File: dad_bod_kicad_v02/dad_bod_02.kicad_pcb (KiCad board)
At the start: 2 copper layers, 79.8 x 79.5 mm, 87 parts, among them J1 Conn_01x01, J10 Conn_01x03_Male, J11 BNC5-J-P-GN-RA-BH2D, J2 Conn_01x01, J3 Conn_01x01, J4 Conn_01x01, J5 BNC5-J-P-GN-RA-BH2D, J6 Conn_02x15_Odd_Even, J7 Conn_01x03_Male, J8 Conn_01x03_Male, K1 EC2-5NU, K2 EC2-5NU, Q1 2N3904, Q2 2N3904, T1 GT07-110-013, U1 SL1002A600SP

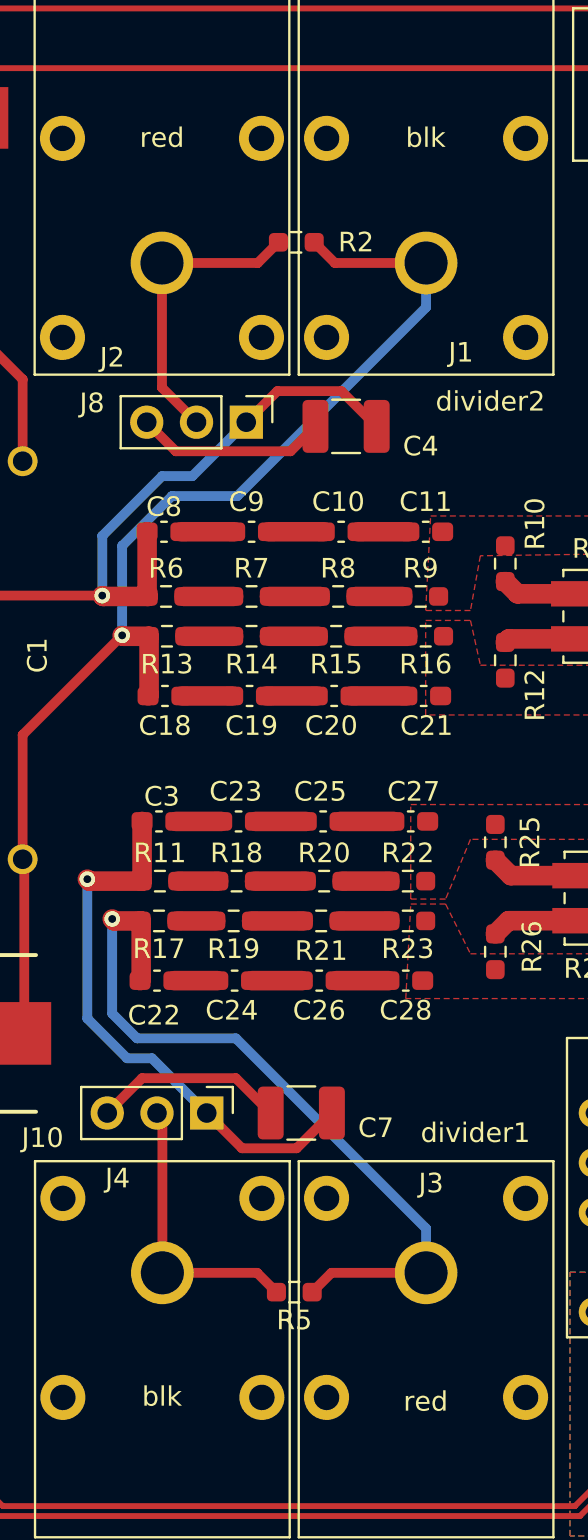
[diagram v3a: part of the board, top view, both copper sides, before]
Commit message: added notes to v02 after build
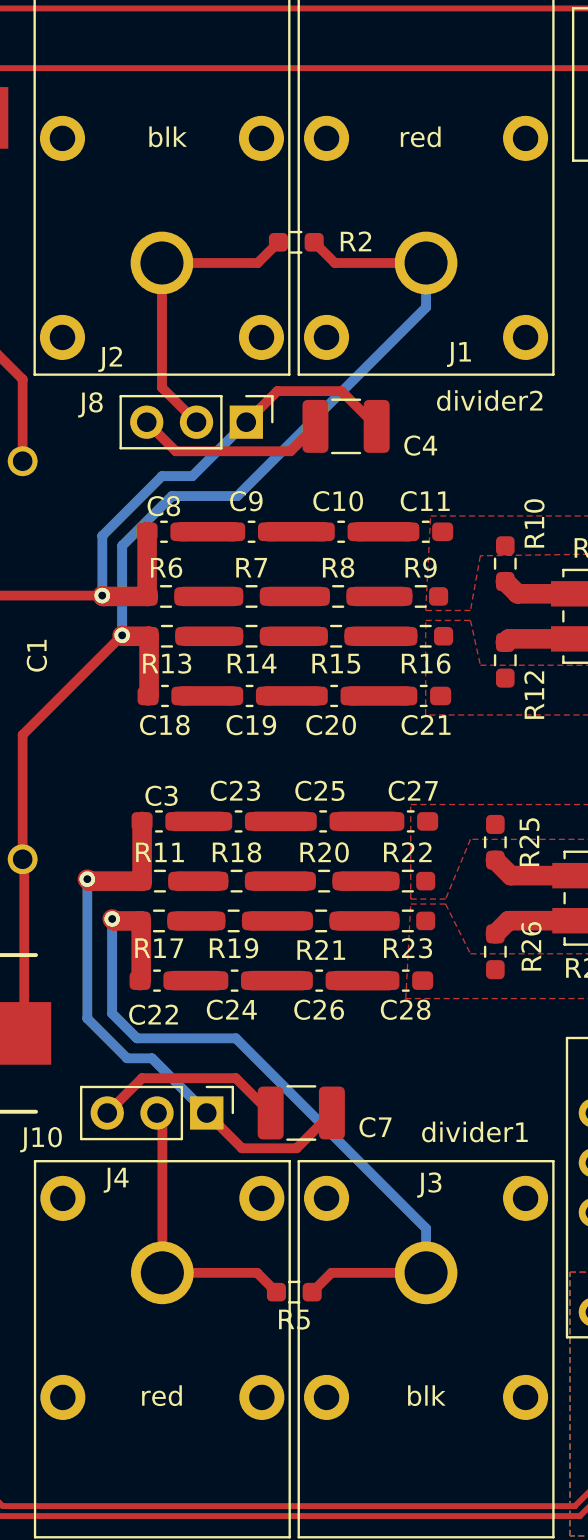
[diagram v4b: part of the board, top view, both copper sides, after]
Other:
- board text added: "corners might need chamfered, 8.5mm"
- board text added: "drill holes for standoffs to attach to case, standoffs need to be at least 13.5mm to clear C1"
- board text added: "increase clearance on dividers"
- board text added: "push header back to match dad"
- board text added: "r2 r5 r27 need 0803"
- board text added: "red/blk have been reversed because this board is flipped upside down when installed"
- board text added: "rotate d1"
- board text added: "translate dad mounting holes to this board, so they can be connected with stand-offs"
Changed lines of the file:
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@@
     (effects (font (size 1 1) (thickness 0.15)) (justify left))
   )
-  (gr_text "blk" (at 134.112 70.866) (layer "F.SilkS")
+  (gr_text "blk" (at 120.904 70.866) (layer "F.SilkS")
     (effects (font (size 1 1) (thickness 0.15)))
   )
@@
     (effects (font (size 1 1) (thickness 0.15)))
   )
-  (gr_text "blk" (at 120.65 135.128) (layer "F.SilkS")
+  (gr_text "blk" (at 134.112 135.128) (layer "F.SilkS")
     (effects (font (size 1 1) (thickness 0.15)))
   )
-  (gr_text "red" (at 120.65 70.866) (layer "F.SilkS")
+  (gr_text "red" (at 133.858 70.866) (layer "F.SilkS")
     (effects (font (size 1 1) (thickness 0.15)))
   )
@@
     (effects (font (size 1 1) (thickness 0.15)))
   )
-  (gr_text "red" (at 134.112 135.382) (layer "F.SilkS")
+  (gr_text "red" (at 120.65 135.128) (layer "F.SilkS")
     (effects (font (size 1 1) (thickness 0.15)))
   )
@@
     (effects (font (size 0.75 0.75) (thickness 0.15)) (justify left))
   )
+  (gr_text "red/blk have been reversed because this board is flipped upside down when installed" (at 207.772 102.362) (layer "Cmts.User")
+    (effects (font (size 1 1) (thickness 0.15)))
+  )
+  (gr_text "translate dad mounting holes to this board, \nso they can be connected with stand-offs" (at 199.39 116.84) (layer "Cmts.User")
+    (effects (font (size 1 1) (thickness 0.15)))
+  )
   (gr_text "the whole header assembly doesnt really need to be on this board\nit can be taken care on the daughter board\njust a thought" (at 203.708 80.772) (layer "Cmts.User")
+    (effects (font (size 1 1) (thickness 0.15)))
+  )
+  (gr_text "corners might need chamfered, 8.5mm" (at 197.358 112.522) (layer "Cmts.User")
+    (effects (font (size 1 1) (thickness 0.15)))
+  )
+  (gr_text "drill holes for standoffs to attach to case, \nstandoffs need to be at least 13.5mm to clear C1" (at 209.55 123.698) (layer "Cmts.User")
     (effects (font (size 1 1) (thickness 0.15)))
   )
@@
     (effects (font (size 1 1) (thickness 0.15)))
   )
+  (gr_text "push header back to match dad" (at 200.152 133.858) (layer "Cmts.User")
+    (effects (font (size 1 1) (thickness 0.15)))
+  )
+  (gr_text "rotate d1" (at 103.378 58.166) (layer "Cmts.User")
+    (effects (font (size 1 1) (thickness 0.15)))
+  )
+  (gr_text "increase clearance on dividers" (at 202.692 139.7) (layer "Cmts.User")
+    (effects (font (size 1 1) (thickness 0.15)))
+  )
   (gr_text "03/20/23" (at 211.582 192.786) (layer "Cmts.User")
     (effects (font (size 1 1) (thickness 0.15)))
   )
+  (gr_text "r2 r5 r27 need 0803" (at 189.484 93.472) (layer "Cmts.User")
+    (effects (font (size 1 1) (thickness 0.15)))
+  )
